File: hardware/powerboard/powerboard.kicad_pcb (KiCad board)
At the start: 4 copper layers, 81.2 x 50.7 mm, 70 parts, among them J1 USB_B_Micro, J10 5V, J11 3V3, J2 Boot, J3 Power, J4 Display, J5 Debug, J6 SPI_1, J7 UART_0, J8 I2C_0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

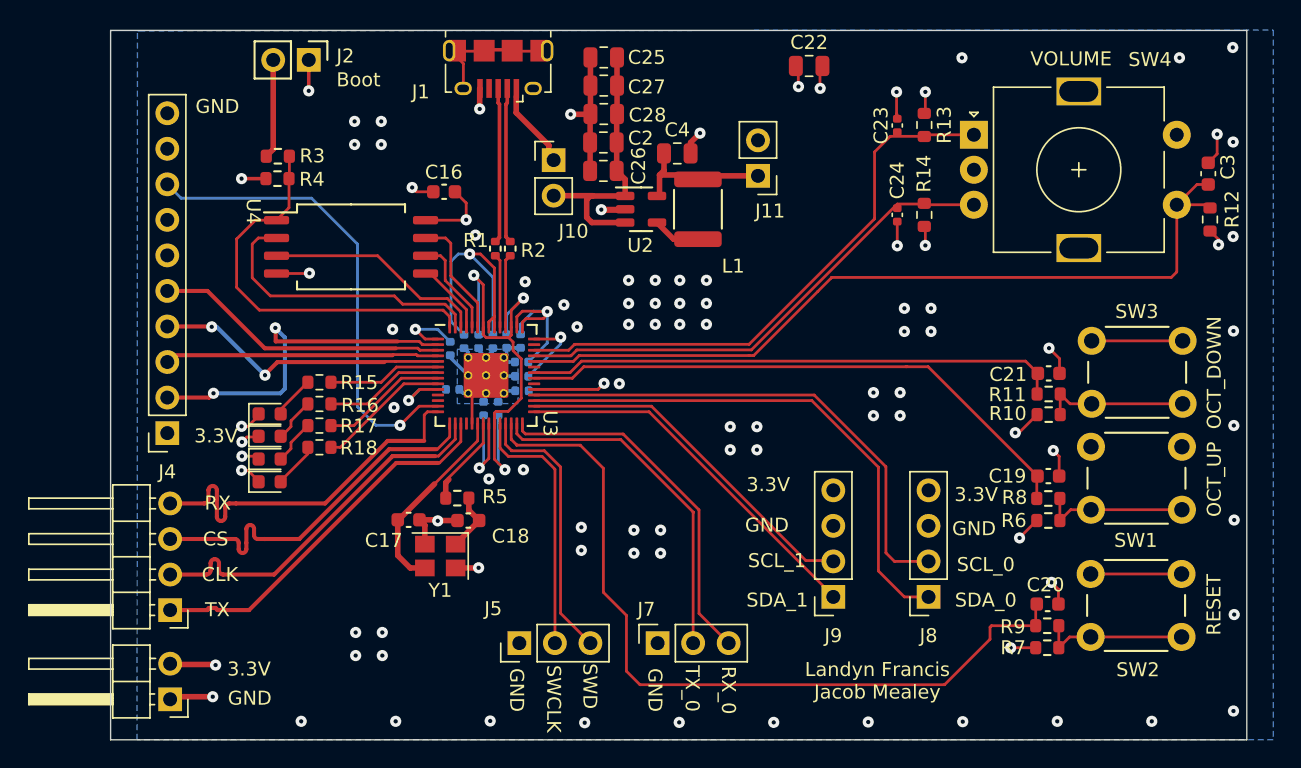
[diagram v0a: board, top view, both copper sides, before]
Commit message: GPIO Added for TFT_DC Display Pin
Connected GPIO 10 to TFT_DC Pin on Display Header
DISPLAY_RESET is now Connected to GPIO 9
pins.h updated accordingly
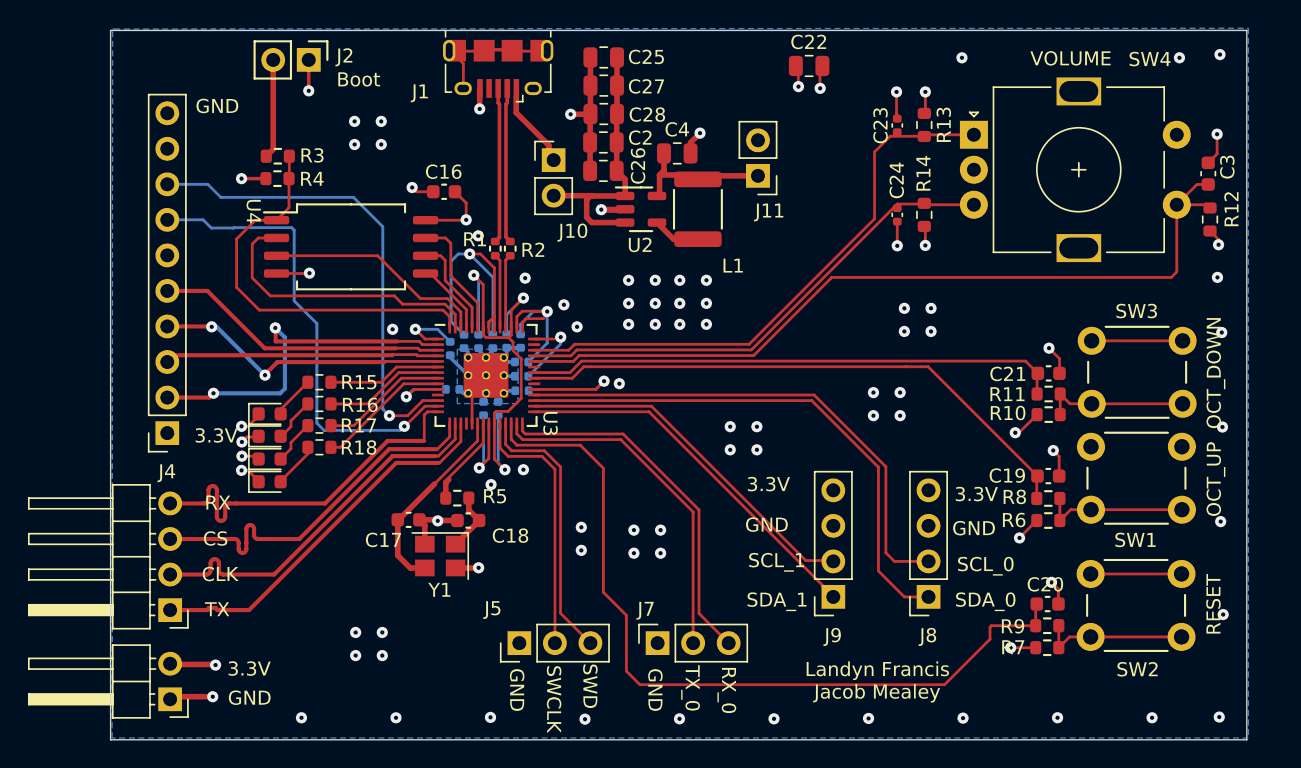
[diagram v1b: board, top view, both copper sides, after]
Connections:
- J4 pad 7: +3.3V -> TFT_DC
- U3 pad 12: unconnected-(U3-Pad12) -> DISPLAY_RESET
- U3 pad 13: DISPLAY_RESET -> TFT_DC
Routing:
- net TFT_DC: track 0.00 -> 33.4 mm, vias 0 -> 1
- net GND: vias 88 -> 86

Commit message: powerboard adjustments, bom added
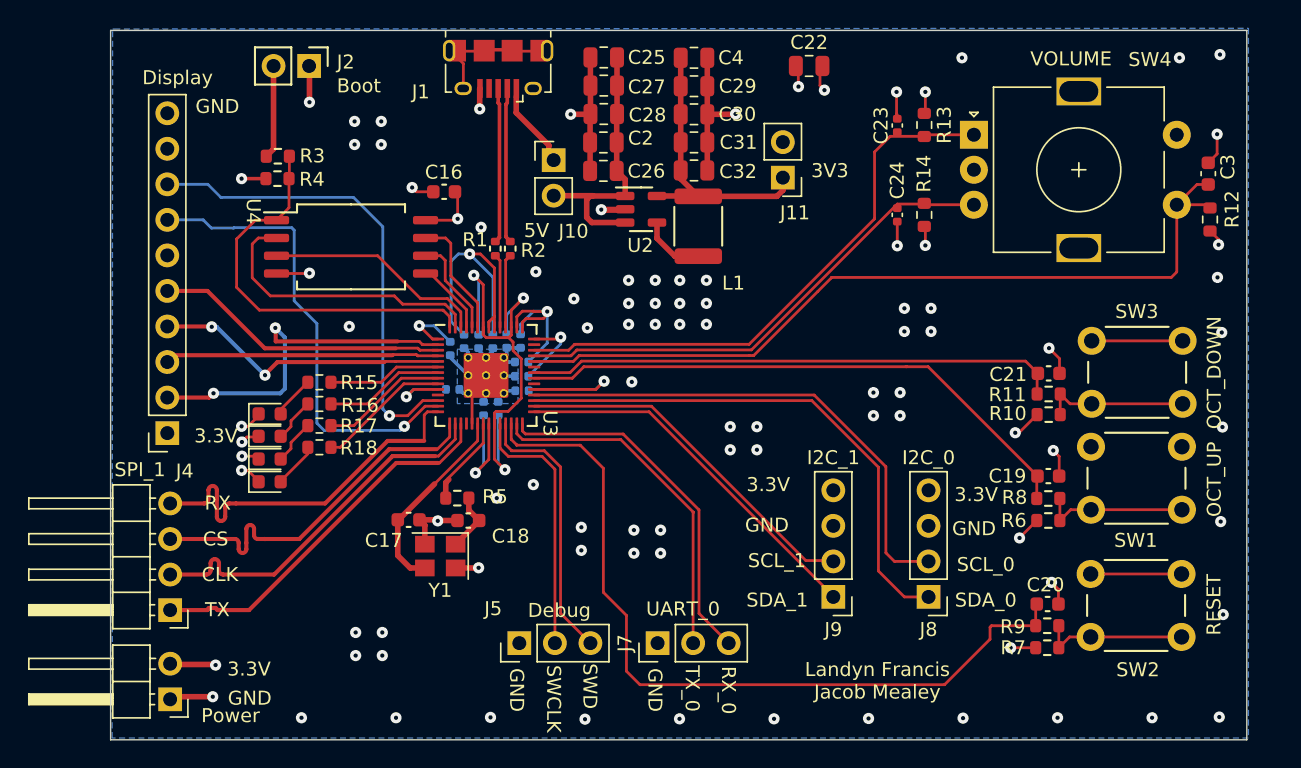
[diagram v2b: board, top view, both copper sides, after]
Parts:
- added C29: 1uF, Capacitor_SMD:C_0805_2012Metric, F.Cu at (90.6, 19.2)
- added C30: 1uF, Capacitor_SMD:C_0805_2012Metric, F.Cu at (90.6, 21.2)
- added C31: 1uF, Capacitor_SMD:C_0805_2012Metric, F.Cu at (90.6, 23.2)
- added C32: 1uF, Capacitor_SMD:C_0805_2012Metric, F.Cu at (90.6, 25.2)
- C4: value 4.7uF -> 1uF
- J7: footprint Connector_PinSocket_2.54mm:PinSocket_1x03_P2.54mm_Vertical -> Connector_PinHeader_2.54mm:PinHeader_1x03_P2.54mm_Vertical
- J8, J9: footprint Connector_PinSocket_2.54mm:PinSocket_1x04_P2.54mm_Vertical -> Connector_PinHeader_2.54mm:PinHeader_1x04_P2.54mm_Vertical
- moved C4 6.94 mm to (90.6, 17.1)
- moved J11 1.78 mm to (96.9, 25.7)
- moved L1 1.21 mm to (90.9, 29.2)
- moved J2 0.43 mm to (63.1, 17.7)
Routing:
- net Net-(J11-Pad1): track 10.5 -> 20.5 mm
- net GND: track 85.0 -> 94.0 mm
- net Net-(L1-Pad1): track 3.42 -> 4.61 mm
- net /~{USB_BOOT}: track 7.41 -> 6.67 mm

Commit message: Powerboard Output Files Pt.1
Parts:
- C3: footprint Capacitor_SMD:C_0603_1608Metric -> Capacitor_SMD:C_0402_1005Metric
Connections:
- C29 pad 1: Net-(J11-Pad1) -> +3.3V
- C30 pad 1: Net-(J11-Pad1) -> +3.3V
- C31 pad 1: Net-(J11-Pad1) -> +3.3V
- C32 pad 1: Net-(J11-Pad1) -> +3.3V
- C4 pad 1: Net-(J11-Pad1) -> +3.3V
- J11 pad 1: Net-(J11-Pad1) -> +3.3V
- L1 pad 2: Net-(J11-Pad1) -> +3.3V
- U2 pad 5: Net-(J11-Pad1) -> +3.3V
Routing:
- net Net-(J11-Pad1): track 20.5 -> 0.00 mm
- net +3.3V: track 88.8 -> 109.3 mm
- net +1V1: track 33.2 -> 31.8 mm
- net GND: track 94.0 -> 94.3 mm, vias 86 -> 104

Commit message: Gerbers and pick and place generated
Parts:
- removed J6: SPI_1, Connector_PinHeader_2.54mm:PinHeader_1x04_P2.54mm_Horizontal
- J3: value Power -> Keysboard Header; footprint Connector_PinHeader_2.54mm:PinHeader_1x02_P2.54mm_Horizontal -> Connector_PinHeader_2.54mm:PinHeader_1x06_P2.54mm_Horizontal
- moved J3 0.84 mm to (53.2, 62.2)

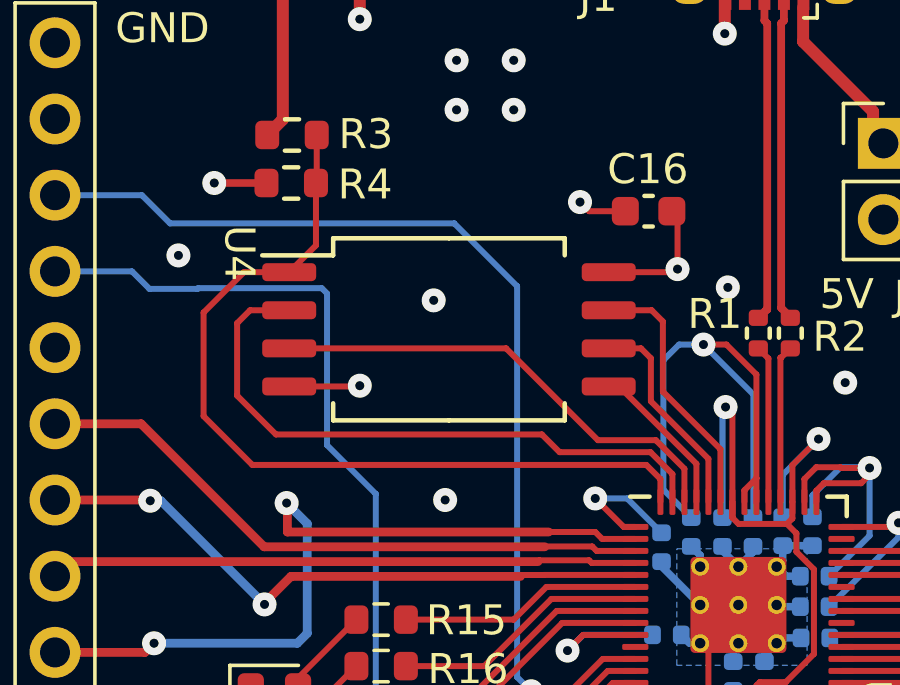
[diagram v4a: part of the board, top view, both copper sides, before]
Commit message: Footprint adjusted for W25QJVSIM FLASH
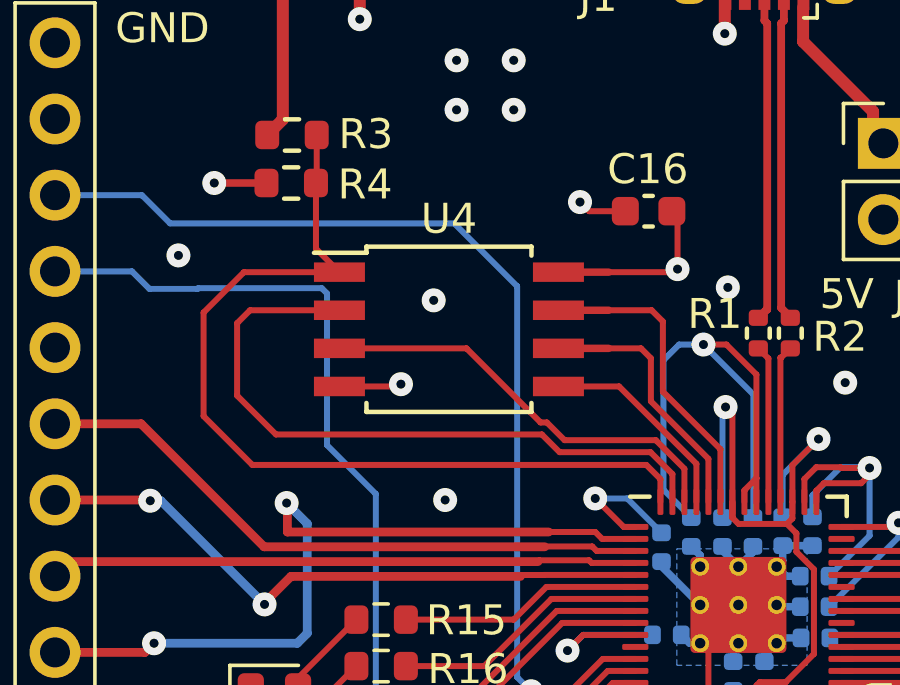
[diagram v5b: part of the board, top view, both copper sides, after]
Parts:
- U4: footprint Package_SO:SOIC-8_7.5x5.85mm_P1.27mm -> Package_SO:SOIC-8W_5.3x5.3mm_P1.27mm
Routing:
- net +3.3V: track 109.8 -> 111.4 mm
- net /QSPI_SD3: track 8.77 -> 10.4 mm
- net /QSPI_SCLK: track 7.12 -> 8.80 mm
- net /QSPI_SD2: track 15.9 -> 14.3 mm
- net /QSPI_SD1: track 20.8 -> 22.5 mm
- net /QSPI_SD0: track 5.26 -> 6.91 mm
- net /QSPI_SS: track 28.7 -> 30.3 mm

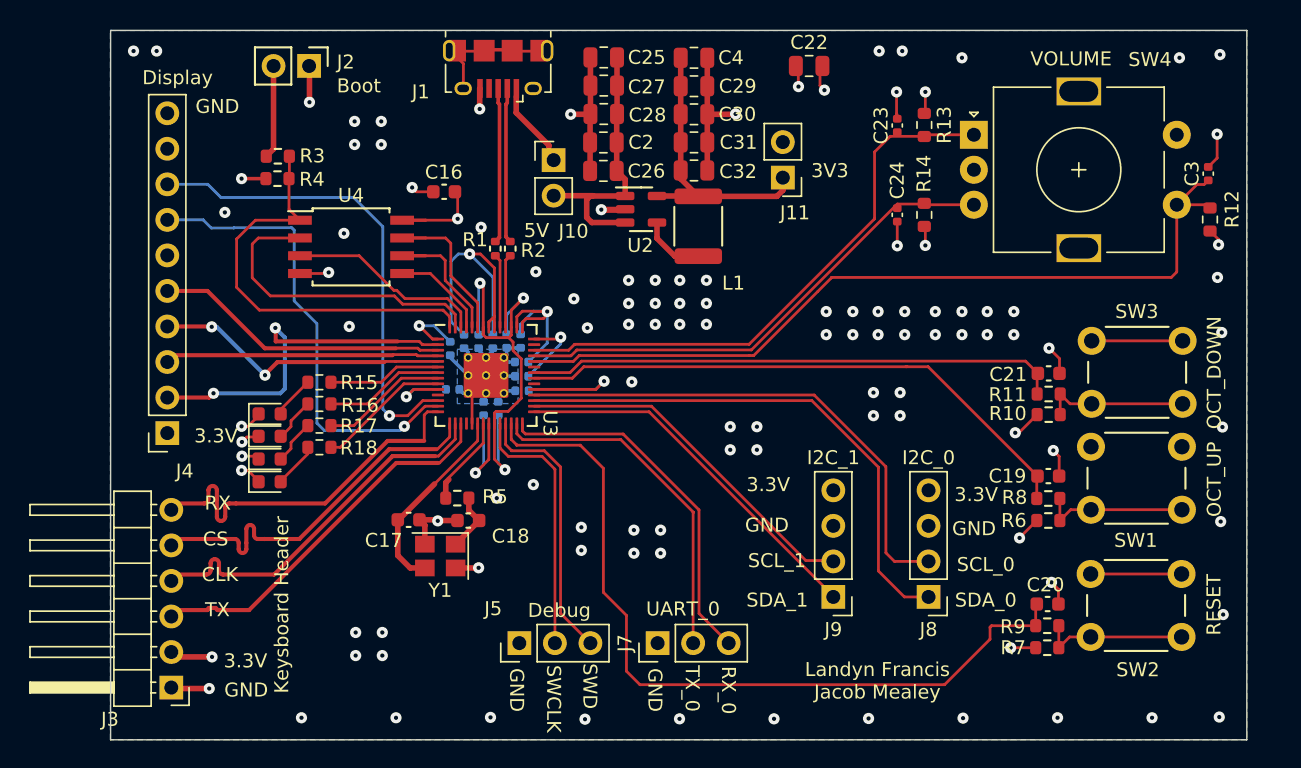
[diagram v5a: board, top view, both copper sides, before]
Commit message: File Cleanup
Folder tracking makes me frown
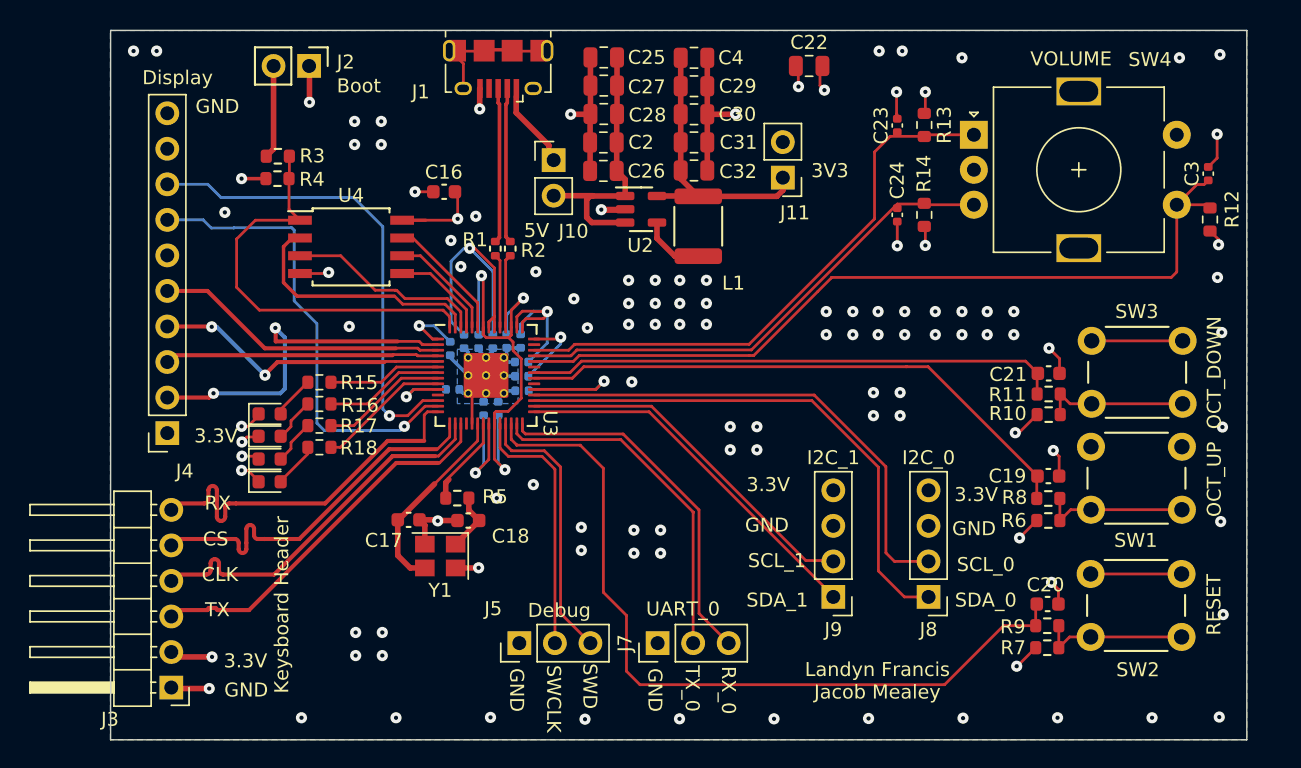
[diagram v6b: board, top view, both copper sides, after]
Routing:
- net /QSPI_SD1: track 22.5 -> 18.1 mm
- net /QSPI_SD3: track 10.4 -> 9.07 mm
- net +1V1: track 31.8 -> 32.9 mm
- net +3.3V: track 111.4 -> 112.3 mm
- net /QSPI_SCLK: track 8.80 -> 7.96 mm
- net RESET: track 57.3 -> 56.8 mm
- net GND: track 94.4 -> 94.1 mm, vias 104 -> 105

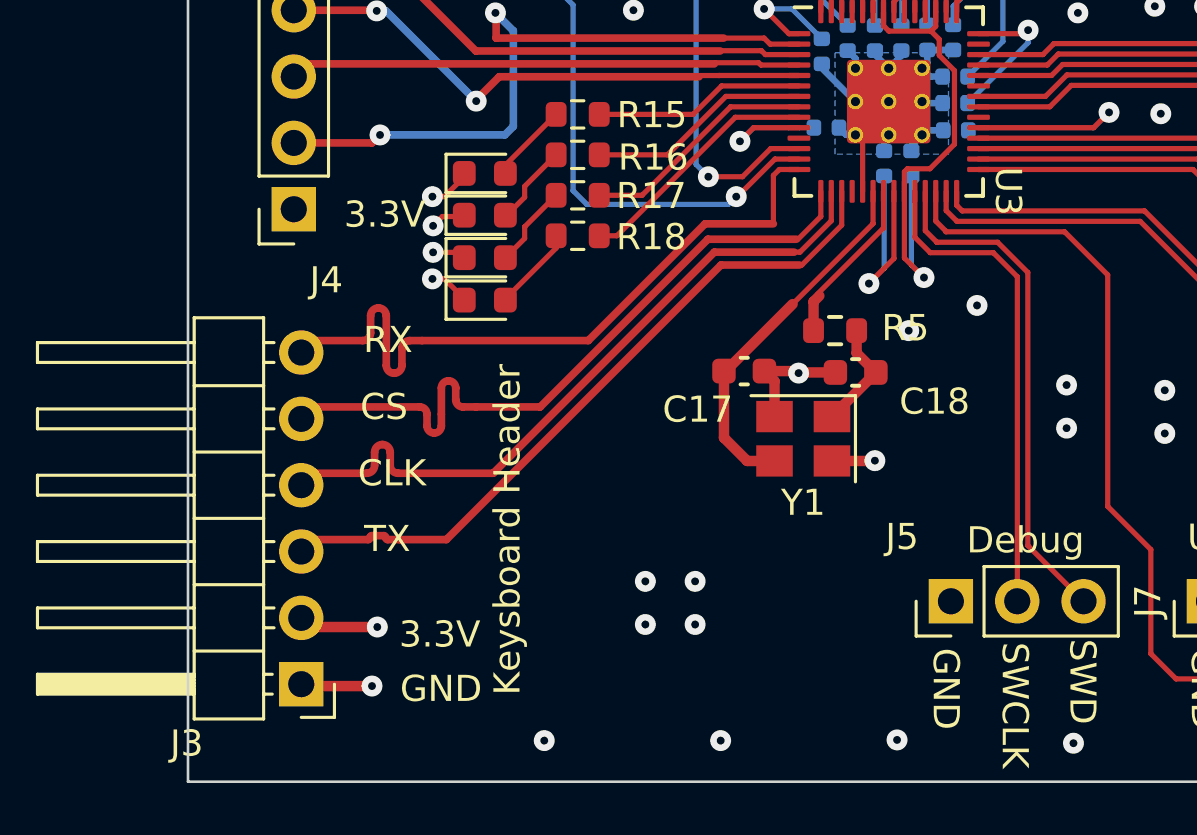
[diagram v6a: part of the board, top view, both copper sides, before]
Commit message: Trying to finalize Powerboard PCB
JLC is being bitchy about the RP2040 and MCP1603, the parts aren't showing up in the part viewer preview window and they are "unselected" for assembly because "coordinate data cannot be found". Very worrying. but as detailed in my message on Discord, I think I have a solution.
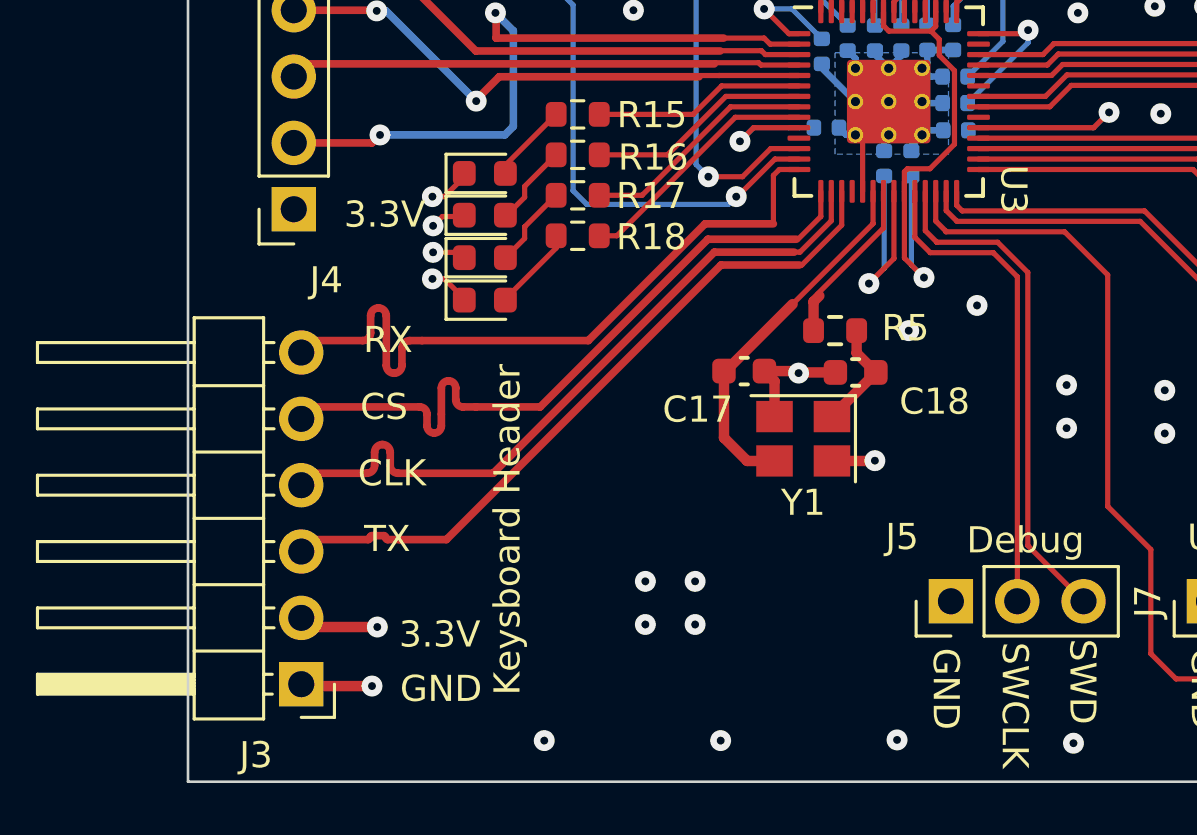
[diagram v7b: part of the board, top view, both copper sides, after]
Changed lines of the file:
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@@
     (property "Sheetname" "")
     (attr through_hole)
-    (fp_text reference "J3" (at 4.385 -2.27) (layer "F.SilkS")
+    (fp_text reference "J3" (at 1.7334 -2.7178) (layer "F.SilkS")
       (effects (font (size 1 1) (thickness 0.15)))
     )
@@
     (property "Sheetname" "")
     (attr smd)
-    (fp_text reference "U3" (at 4.572 3.429 -90 unlocked) (layer "F.SilkS")
-      (effects (font (size 1 1) (thickness 0.15)))
-    )
+    (fp_text reference "U3" (at 4.7782 3.35975 -90 unlocked) (layer "F.SilkS")
+      (effects (font (size 1 1) (thickness 0.15)))
+    )
